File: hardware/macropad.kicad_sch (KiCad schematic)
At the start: 21 parts, among them J1 Conn_01x04, J2 Conn_01x06, SW1 SW_Push, SW10 RotaryEncoder_Switch, SW2 SW_Push, SW3 SW_Push, SW4 SW_Push, SW5 SW_Push, SW6 SW_Push, SW7 SW_Push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

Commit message: :sparkles: Add pico & screen
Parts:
- removed SW10: RotaryEncoder_Switch, 4ms_Encoder:ENC_SPST_12mm, symbol Device:RotaryEncoder_Switch
- added J3: Screen connector, Connector_PinHeader_2.54mm:PinHeader_1x04_P2.54mm_Vertical, symbol Connector_Generic:Conn_01x04
- added U1: Pico, MCU_RaspberryPi_and_Boards:RPi_Pico_SMD_TH, symbol MCU_RaspberryPi_and_Boards:Pico
- J1: value Conn_01x04 -> Screen
- J2: footprint Connector_PinHeader_2.54mm:PinHeader_1x06_P2.54mm_Horizontal -> Connector_PinHeader_2.54mm:PinHeader_1x06_P2.54mm_Vertical
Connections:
- net COL1: now also U1.9 (GPIO6)
- net COL2: now also U1.10 (GPIO7)
- net COL3: now also U1.11 (GPIO8)
- net GND: now also J3.2 (Pin_2), U1.13 (GND), U1.18 (GND), U1.23 (GND), U1.28 (GND), U1.3 (GND), U1.33 (AGND), U1.38 (GND), U1.42 (GND), U1.8 (GND)
- net ROW1: now also U1.12 (GPIO9)
- net ROW2: now also U1.14 (GPIO10)
- net ROW3: now also U1.15 (GPIO11)
- net SCK: now also J3.3 (Pin_3), U1.32 (GPIO27_ADC1)
- net SDA: now also J3.4 (Pin_4), U1.31 (GPIO26_ADC0)
- net VDD renamed 3V3
- net 3V3: now also J3.1 (Pin_1), U1.36 (3V3)

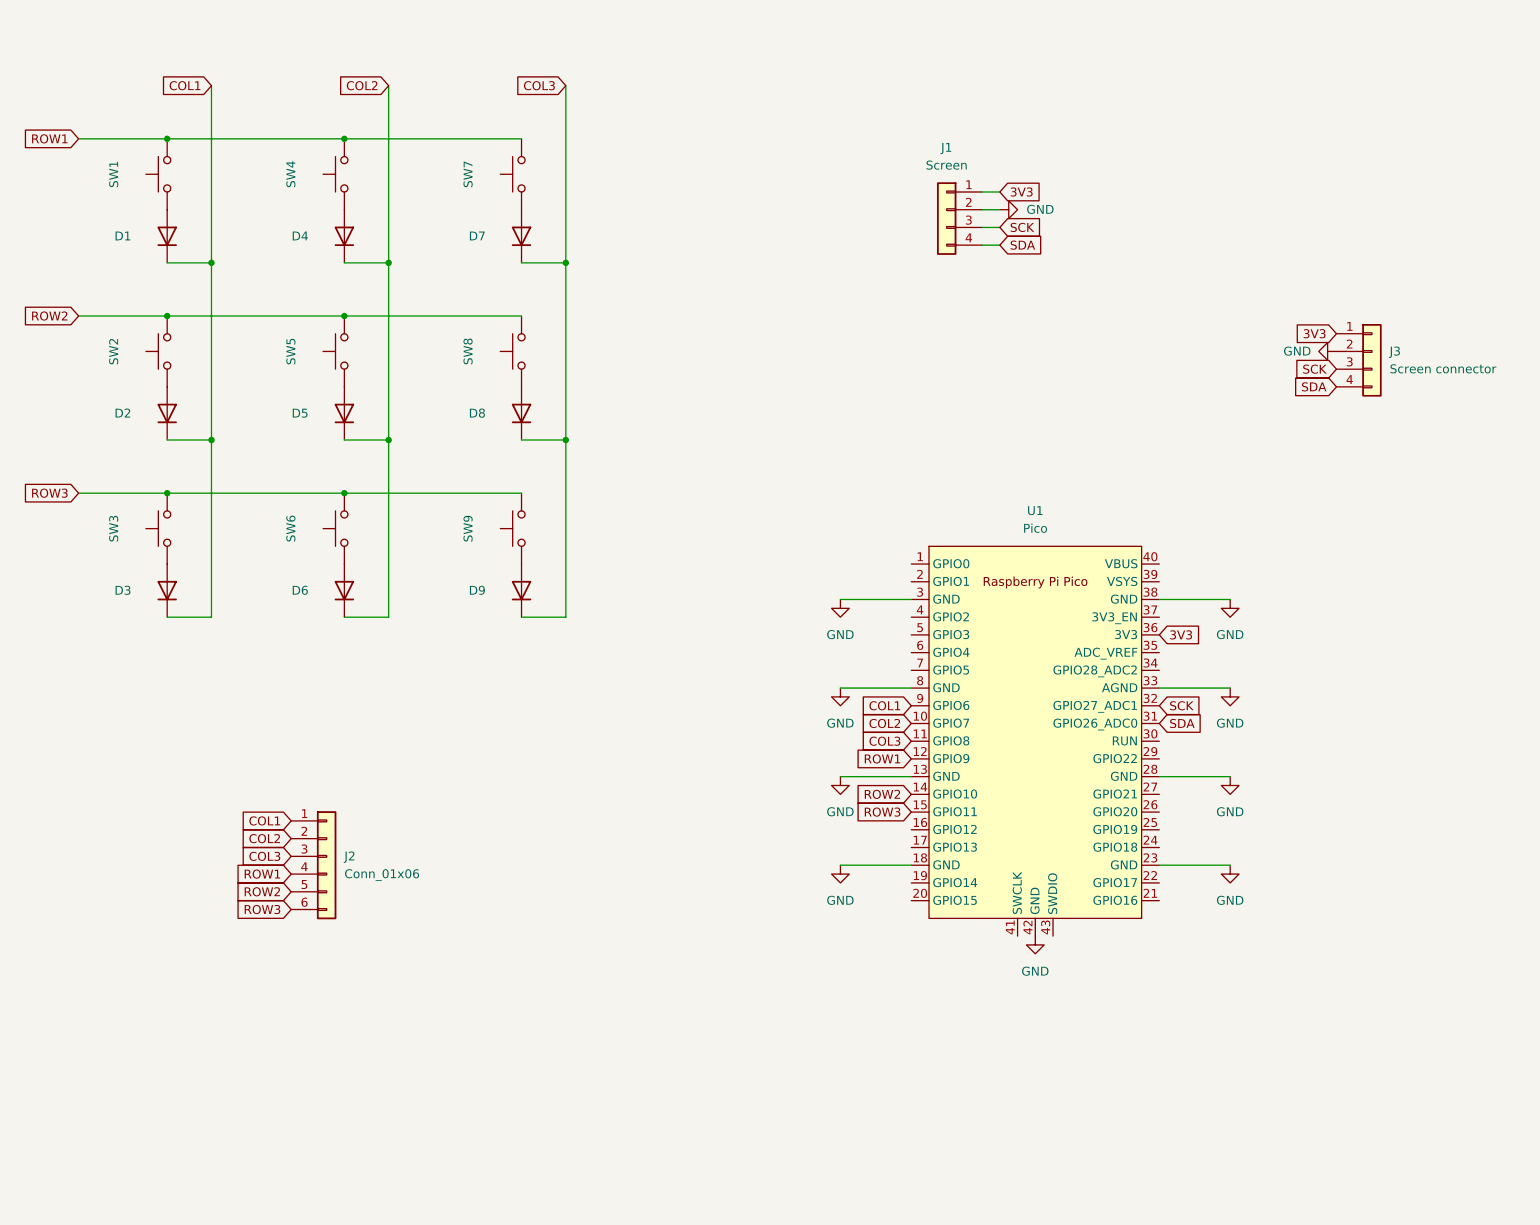
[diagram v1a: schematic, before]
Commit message: :construction: Add headers for SPI screen also
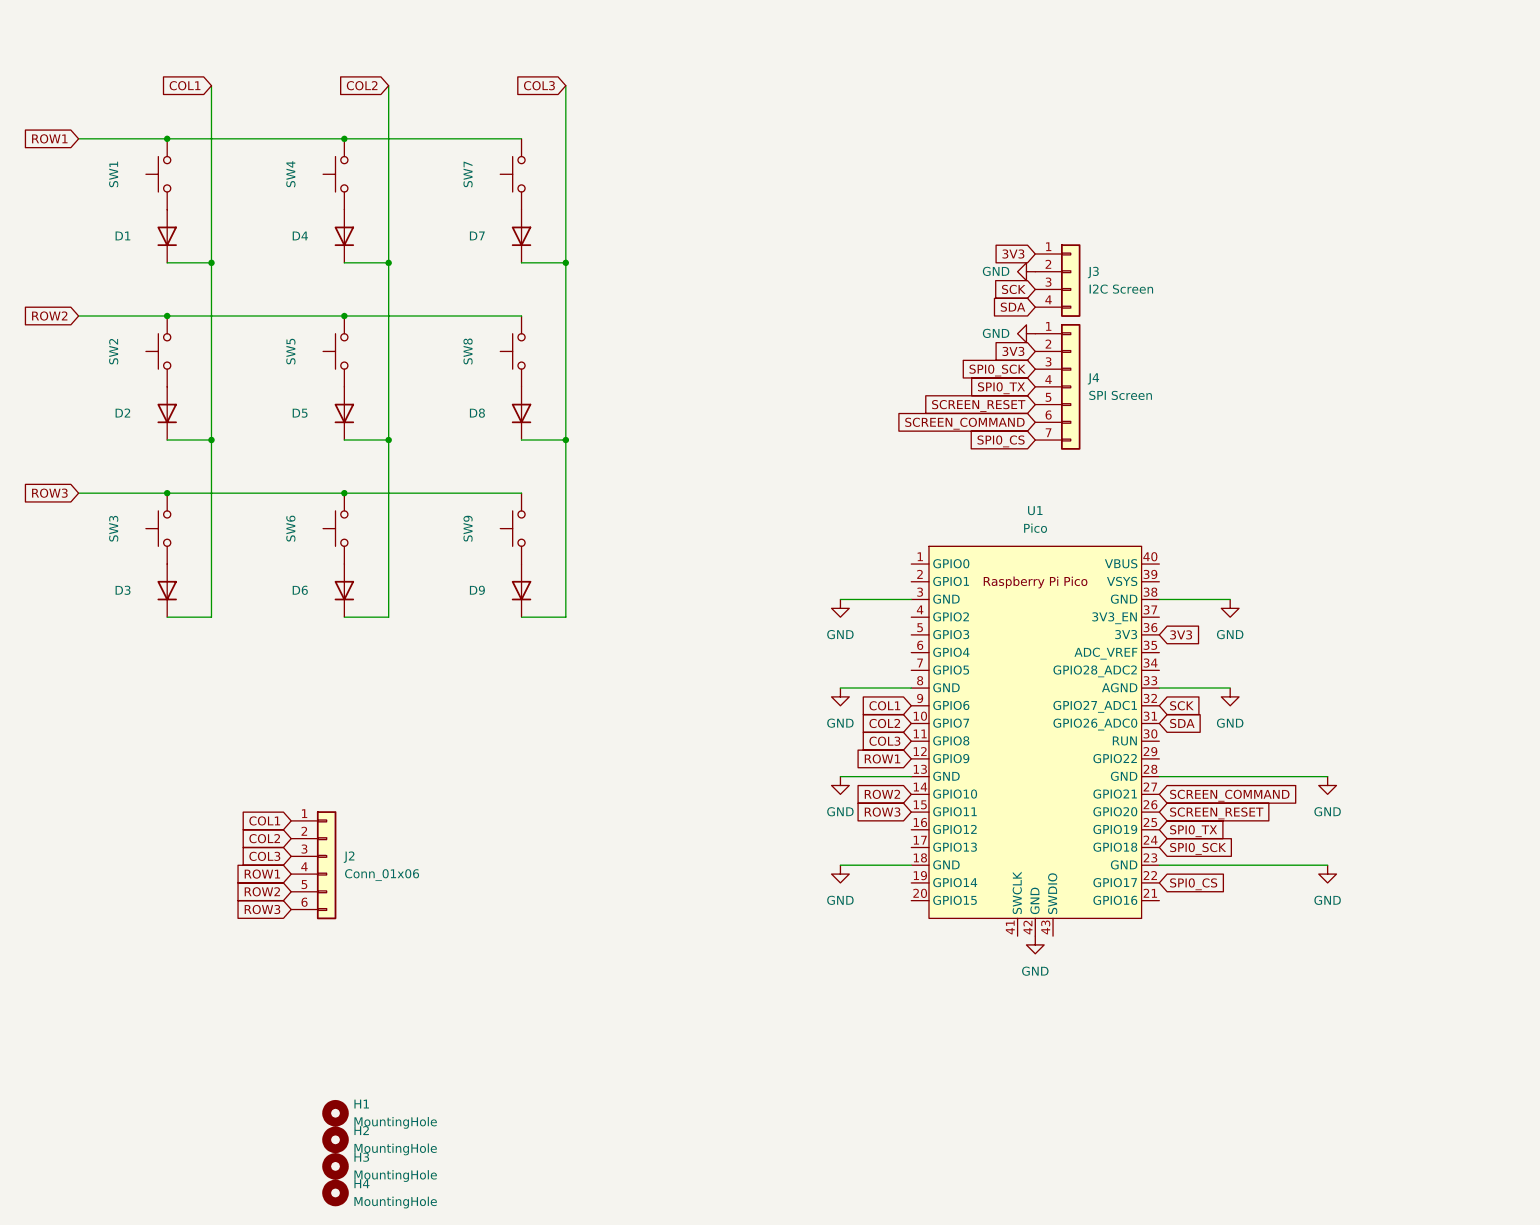
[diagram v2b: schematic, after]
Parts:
- removed J1: Screen, nn_lib:I2C_1.3inch_OLED, symbol Connector_Generic:Conn_01x04
- added H1, H2, H3, H4: MountingHole, MountingHole:MountingHole_3.2mm_M3, symbol Mechanical:MountingHole
- added J4: SPI Screen, Connector_PinHeader_2.54mm:PinHeader_1x07_P2.54mm_Vertical, symbol Connector_Generic:Conn_01x07
- J3: value Screen connector -> I2C Screen
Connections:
- net 3V3: now also J4.2 (Pin_2)
- net GND: now also J4.1 (Pin_1)
- net SPI0_CS: now reaches U1.22 (GPIO17)
- net SPI0_CS: now also J4.7 (Pin_7)
- net SPI0_SCK: now reaches U1.24 (GPIO18)
- net SPI0_SCK: now also J4.3 (Pin_3)
- net SPI0_TX: now reaches U1.25 (GPIO19)
- net SPI0_TX: now also J4.4 (Pin_4)
- net SCREEN_RESET: now reaches U1.26 (GPIO20)
- net SCREEN_RESET: now also J4.5 (Pin_5)
- net SCREEN_COMMAND: now reaches U1.27 (GPIO21)
- net SCREEN_COMMAND: now also J4.6 (Pin_6)
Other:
- moved on the sheet: J3
